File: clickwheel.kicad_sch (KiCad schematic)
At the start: 4 parts

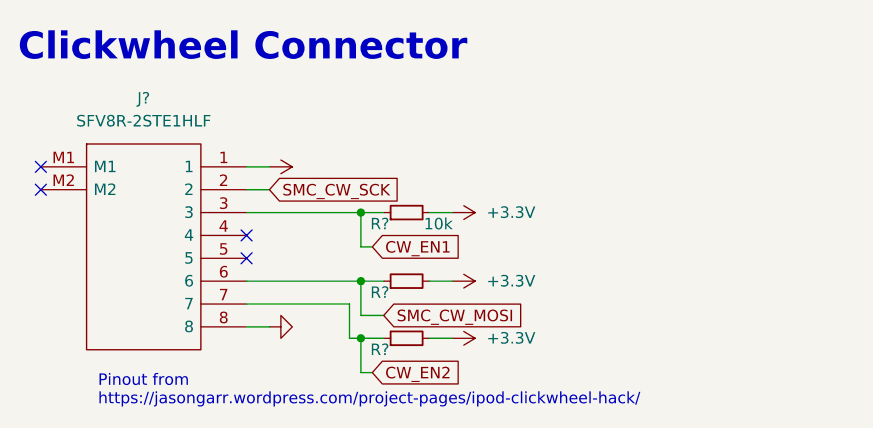
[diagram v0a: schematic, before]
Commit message: schem: first pass done, ERC passing
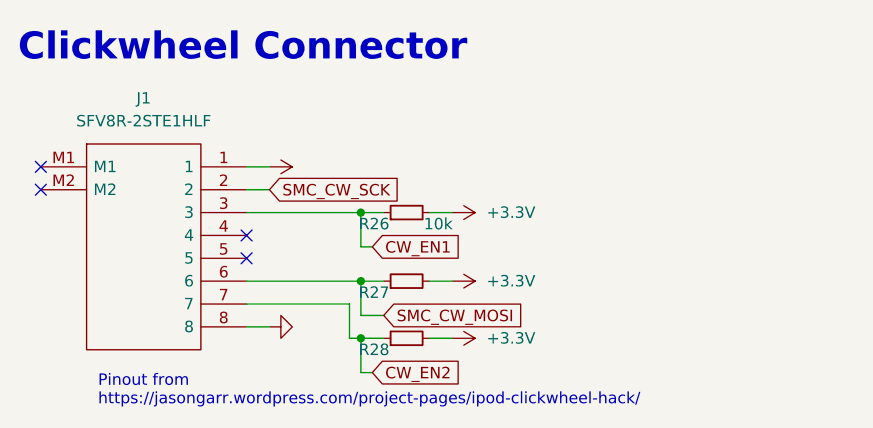
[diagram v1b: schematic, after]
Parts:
- gave numbers to parts that had none: 4
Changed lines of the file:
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@@
   (no_connect (at 95.25 88.9))
   (no_connect (at 95.25 91.44))
+  (no_connect (at 118.11 96.52))
   (no_connect (at 118.11 99.06))
-  (no_connect (at 118.11 96.52))
   (wire (pts (xy 132.08 111.76) (xy 130.81 111.76))
     (stroke (width 0) (type default) (color 0 0 0 0))
@@
   (symbol (lib_id "power:+3.3V") (at 140.97 93.98 270) (unit 1)
     (in_bom yes) (on_board yes) (fields_autoplaced)
-    (property "Reference" "#PWR?" (id 0) (at 137.16 93.98 0)
+    (property "Reference" "#PWR063" (id 0) (at 137.16 93.98 0)
       (effects (font (size 1.27 1.27)) hide)
     )
@@
   (symbol (lib_id "power:GND") (at 120.65 106.68 90) (unit 1)
     (in_bom yes) (on_board yes) (fields_autoplaced)
-    (property "Reference" "#PWR?" (id 0) (at 127 106.68 0)
+    (property "Reference" "#PWR062" (id 0) (at 127 106.68 0)
       (effects (font (size 1.27 1.27)) hide)
     )
@@
   (symbol (lib_id "Device:R_Small") (at 135.89 93.98 90) (unit 1)
     (in_bom yes) (on_board yes)
-    (property "Reference" "R?" (id 0) (at 133.985 95.25 90)
+    (property "Reference" "R26" (id 0) (at 133.985 95.25 90)
       (effects (font (size 1.27 1.27)) (justify left))
     )
@@
   (symbol (lib_id "Device:R_Small") (at 135.89 107.95 90) (unit 1)
     (in_bom yes) (on_board yes)
-    (property "Reference" "R?" (id 0) (at 133.985 109.22 90)
+    (property "Reference" "R28" (id 0) (at 133.985 109.22 90)
       (effects (font (size 1.27 1.27)) (justify left))
     )
@@
   (symbol (lib_id "gigahawk:SFV8R-2STE1HLF") (at 95.25 88.9 0) (unit 1)
     (in_bom yes) (on_board yes) (fields_autoplaced)
-    (property "Reference" "J?" (id 0) (at 106.68 81.28 0))
+    (property "Reference" "J1" (id 0) (at 106.68 81.28 0))
     (property "Value" "SFV8R-2STE1HLF" (id 1) (at 106.68 83.82 0))
     (property "Footprint" "Gigahawk:SFV8R2STE1HLF" (id 2) (at 114.3 86.36 0)
@@
   (symbol (lib_id "power:+3.3V") (at 120.65 88.9 270) (unit 1)
     (in_bom yes) (on_board yes) (fields_autoplaced)
-    (property "Reference" "#PWR?" (id 0) (at 116.84 88.9 0)
+    (property "Reference" "#PWR061" (id 0) (at 116.84 88.9 0)
       (effects (font (size 1.27 1.27)) hide)
     )
@@
   (symbol (lib_id "power:+3.3V") (at 140.97 101.6 270) (unit 1)
     (in_bom yes) (on_board yes) (fields_autoplaced)
-    (property "Reference" "#PWR?" (id 0) (at 137.16 101.6 0)
+    (property "Reference" "#PWR064" (id 0) (at 137.16 101.6 0)
       (effects (font (size 1.27 1.27)) hide)
     )
@@
   (symbol (lib_id "power:+3.3V") (at 140.97 107.95 270) (unit 1)
     (in_bom yes) (on_board yes) (fields_autoplaced)
-    (property "Reference" "#PWR?" (id 0) (at 137.16 107.95 0)
+    (property "Reference" "#PWR065" (id 0) (at 137.16 107.95 0)
       (effects (font (size 1.27 1.27)) hide)
     )
@@
   (symbol (lib_id "Device:R_Small") (at 135.89 101.6 90) (unit 1)
     (in_bom yes) (on_board yes)
-    (property "Reference" "R?" (id 0) (at 133.985 102.87 90)
-      (effects (font (size 1.27 1.27)) (justify left))
-    )
+    (property "Reference" "R27" (id 0) (at 133.985 102.87 90)
+      (effects (font (size 1.27 1.27)) (justify left))
+    )

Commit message: analysis: specify pi will be powered directly from VCC
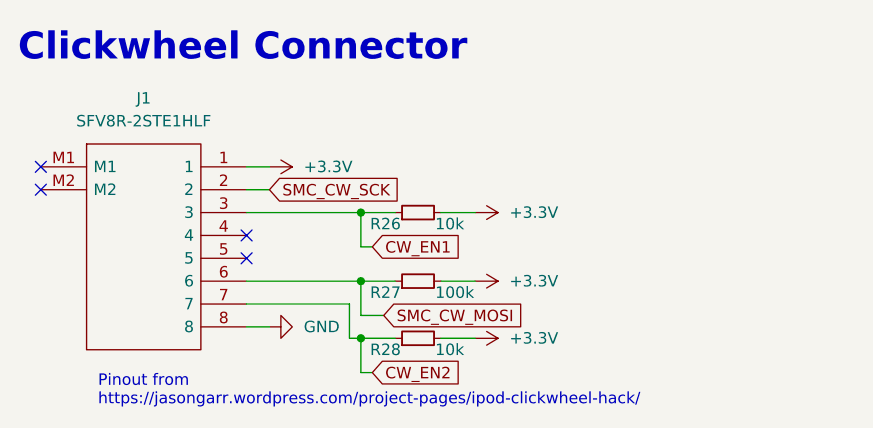
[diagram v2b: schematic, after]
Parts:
- R26: footprint (none) -> Resistor_SMD:R_0402_1005Metric
- R27: value (none) -> 100k; footprint (none) -> Resistor_SMD:R_0402_1005Metric
- R28: value (none) -> 10k; footprint (none) -> Resistor_SMD:R_0402_1005Metric
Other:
- moved on the sheet: R26, R27, R28
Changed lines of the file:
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@@
 (kicad_sch (version 20211123) (generator eeschema)
   (paper "A4")
+  (junction (at 130.81 107.95) (diameter 0) (color 0 0 0 0)
+  )
   (junction (at 130.81 93.98) (diameter 0) (color 0 0 0 0)
   )
   (junction (at 130.81 101.6) (diameter 0) (color 0 0 0 0)
-  )
-  (junction (at 130.81 107.95) (diameter 0) (color 0 0 0 0)
   )
   (no_connect (at 95.25 88.9))
@@
     (stroke (width 0) (type default) (color 0 0 0 0))
   )
-  (wire (pts (xy 130.81 101.6) (xy 133.35 101.6))
-    (stroke (width 0) (type default) (color 0 0 0 0))
-  )
-  (wire (pts (xy 129.54 107.95) (xy 130.81 107.95))
-    (stroke (width 0) (type default) (color 0 0 0 0))
-  )
-  (wire (pts (xy 130.81 93.98) (xy 133.35 93.98))
-    (stroke (width 0) (type default) (color 0 0 0 0))
-  )
-  (wire (pts (xy 138.43 107.95) (xy 140.97 107.95))
+  (wire (pts (xy 130.81 101.6) (xy 134.62 101.6))
+    (stroke (width 0) (type default) (color 0 0 0 0))
+  )
+  (wire (pts (xy 130.81 107.95) (xy 129.54 107.95))
+    (stroke (width 0) (type default) (color 0 0 0 0))
+  )
+  (wire (pts (xy 130.81 93.98) (xy 134.62 93.98))
+    (stroke (width 0) (type default) (color 0 0 0 0))
+  )
+  (wire (pts (xy 139.7 107.95) (xy 143.51 107.95))
     (stroke (width 0) (type default) (color 0 0 0 0))
   )
@@
     (stroke (width 0) (type default) (color 0 0 0 0))
   )
+  (wire (pts (xy 130.81 107.95) (xy 134.62 107.95))
+    (stroke (width 0) (type default) (color 0 0 0 0))
+  )
   (wire (pts (xy 130.81 97.79) (xy 130.81 93.98))
     (stroke (width 0) (type default) (color 0 0 0 0))
   )
-  (wire (pts (xy 138.43 93.98) (xy 140.97 93.98))
-    (stroke (width 0) (type default) (color 0 0 0 0))
-  )
-  (wire (pts (xy 138.43 101.6) (xy 140.97 101.6))
+  (wire (pts (xy 139.7 93.98) (xy 143.51 93.98))
+    (stroke (width 0) (type default) (color 0 0 0 0))
+  )
+  (wire (pts (xy 139.7 101.6) (xy 143.51 101.6))
     (stroke (width 0) (type default) (color 0 0 0 0))
   )
@@
   )
   (wire (pts (xy 118.11 104.14) (xy 129.54 104.14))
-    (stroke (width 0) (type default) (color 0 0 0 0))
-  )
-  (wire (pts (xy 130.81 107.95) (xy 133.35 107.95))
     (stroke (width 0) (type default) (color 0 0 0 0))
   )
@@
     )
   )
-  (symbol (lib_id "power:+3.3V") (at 140.97 93.98 270) (unit 1)
-    (in_bom yes) (on_board yes) (fields_autoplaced)
-    (property "Reference" "#PWR063" (id 0) (at 137.16 93.98 0)
-      (effects (font (size 1.27 1.27)) hide)
-    )
-    (property "Value" "+3.3V" (id 1) (at 144.78 93.9799 90)
-      (effects (font (size 1.27 1.27)) (justify left))
-    )
-    (property "Footprint" "" (id 2) (at 140.97 93.98 0)
-      (effects (font (size 1.27 1.27)) hide)
-    )
-    (property "Datasheet" "" (id 3) (at 140.97 93.98 0)
+  (symbol (lib_id "power:+3.3V") (at 143.51 93.98 270) (unit 1)
+    (in_bom yes) (on_board yes) (fields_autoplaced)
+    (property "Reference" "#PWR063" (id 0) (at 139.7 93.98 0)
+      (effects (font (size 1.27 1.27)) hide)
+    )
+    (property "Value" "+3.3V" (id 1) (at 147.32 93.9799 90)
+      (effects (font (size 1.27 1.27)) (justify left))
+    )
+    (property "Footprint" "" (id 2) (at 143.51 93.98 0)
+      (effects (font (size 1.27 1.27)) hide)
+    )
+    (property "Datasheet" "" (id 3) (at 143.51 93.98 0)
       (effects (font (size 1.27 1.27)) hide)
     )
@@
       (effects (font (size 1.27 1.27)) hide)
     )
-    (property "Value" "" (id 1) (at 124.46 106.6799 90)
+    (property "Value" "GND" (id 1) (at 124.46 106.6799 90)
       (effects (font (size 1.27 1.27)) (justify right))
     )
@@
     (pin "1")
   )
-  (symbol (lib_id "Device:R_Small") (at 135.89 93.98 90) (unit 1)
+  (symbol (lib_id "Device:R_Small") (at 137.16 93.98 90) (unit 1)
     (in_bom yes) (on_board yes)
-    (property "Reference" "R26" (id 0) (at 133.985 95.25 90)
-      (effects (font (size 1.27 1.27)) (justify left))
-    )
-    (property "Value" "10k" (id 1) (at 137.795 95.25 90)
-      (effects (font (size 1.27 1.27)) (justify right))
-    )
-    (property "Footprint" "" (id 2) (at 135.89 93.98 0)
-      (effects (font (size 1.27 1.27)) hide)
-    )
-    (property "Datasheet" "~" (id 3) (at 135.89 93.98 0)
+    (property "Reference" "R26" (id 0) (at 135.255 95.25 90)
+      (effects (font (size 1.27 1.27)) (justify left))
+    )
+    (property "Value" "10k" (id 1) (at 139.065 95.25 90)
+      (effects (font (size 1.27 1.27)) (justify right))
+    )
+    (property "Footprint" "Resistor_SMD:R_0402_1005Metric" (id 2) (at 137.16 93.98 0)
+      (effects (font (size 1.27 1.27)) hide)
+    )
+    (property "Datasheet" "~" (id 3) (at 137.16 93.98 0)
       (effects (font (size 1.27 1.27)) hide)
     )
@@
     (pin "2")
   )
-  (symbol (lib_id "Device:R_Small") (at 135.89 107.95 90) (unit 1)
+  (symbol (lib_id "Device:R_Small") (at 137.16 107.95 90) (unit 1)
     (in_bom yes) (on_board yes)
-    (property "Reference" "R28" (id 0) (at 133.985 109.22 90)
-      (effects (font (size 1.27 1.27)) (justify left))
-    )
-    (property "Value" "" (id 1) (at 137.795 109.22 90)
-      (effects (font (size 1.27 1.27)) (justify right))
-    )
-    (property "Footprint" "" (id 2) (at 135.89 107.95 0)
-      (effects (font (size 1.27 1.27)) hide)
-    )
-    (property "Datasheet" "~" (id 3) (at 135.89 107.95 0)
+    (property "Reference" "R28" (id 0) (at 135.255 109.22 90)
+      (effects (font (size 1.27 1.27)) (justify left))
+    )
+    (property "Value" "10k" (id 1) (at 139.065 109.22 90)
+      (effects (font (size 1.27 1.27)) (justify right))
+    )
+    (property "Footprint" "Resistor_SMD:R_0402_1005Metric" (id 2) (at 137.16 107.95 0)
+      (effects (font (size 1.27 1.27)) hide)
+    )
+    (property "Datasheet" "~" (id 3) (at 137.16 107.95 0)
       (effects (font (size 1.27 1.27)) hide)
     )
@@
       (effects (font (size 1.27 1.27)) hide)
     )
-    (property "Value" "" (id 1) (at 124.46 88.8999 90)
+    (property "Value" "+3.3V" (id 1) (at 124.46 88.8999 90)
       (effects (font (size 1.27 1.27)) (justify left))
     )
@@
     (pin "1")
   )
-  (symbol (lib_id "power:+3.3V") (at 140.97 101.6 270) (unit 1)
-    (in_bom yes) (on_board yes) (fields_autoplaced)
-    (property "Reference" "#PWR064" (id 0) (at 137.16 101.6 0)
-      (effects (font (size 1.27 1.27)) hide)
-    )
-    (property "Value" "+3.3V" (id 1) (at 144.78 101.5999 90)
-      (effects (font (size 1.27 1.27)) (justify left))
-    )
-    (property "Footprint" "" (id 2) (at 140.97 101.6 0)
-      (effects (font (size 1.27 1.27)) hide)
-    )
-    (property "Datasheet" "" (id 3) (at 140.97 101.6 0)
-      (effects (font (size 1.27 1.27)) hide)
-    )
-    (pin "1")
-  )
-  (symbol (lib_id "power:+3.3V") (at 140.97 107.95 270) (unit 1)
-    (in_bom yes) (on_board yes) (fields_autoplaced)
-    (property "Reference" "#PWR065" (id 0) (at 137.16 107.95 0)
-      (effects (font (size 1.27 1.27)) hide)
-    )
-    (property "Value" "+3.3V" (id 1) (at 144.78 107.9499 90)
-      (effects (font (size 1.27 1.27)) (justify left))
-    )
-    (property "Footprint" "" (id 2) (at 140.97 107.95 0)
-      (effects (font (size 1.27 1.27)) hide)
-    )
-    (property "Datasheet" "" (id 3) (at 140.97 107.95 0)
-      (effects (font (size 1.27 1.27)) hide)
-    )
-    (pin "1")
-  )
-  (symbol (lib_id "Device:R_Small") (at 135.89 101.6 90) (unit 1)
+  (symbol (lib_id "power:+3.3V") (at 143.51 101.6 270) (unit 1)
+    (in_bom yes) (on_board yes) (fields_autoplaced)
+    (property "Reference" "#PWR064" (id 0) (at 139.7 101.6 0)
+      (effects (font (size 1.27 1.27)) hide)
+    )
+    (property "Value" "+3.3V" (id 1) (at 147.32 101.5999 90)
+      (effects (font (size 1.27 1.27)) (justify left))
+    )
+    (property "Footprint" "" (id 2) (at 143.51 101.6 0)
+      (effects (font (size 1.27 1.27)) hide)
+    )
+    (property "Datasheet" "" (id 3) (at 143.51 101.6 0)
+      (effects (font (size 1.27 1.27)) hide)
+    )
+    (pin "1")
+  )
+  (symbol (lib_id "power:+3.3V") (at 143.51 107.95 270) (unit 1)
+    (in_bom yes) (on_board yes) (fields_autoplaced)
+    (property "Reference" "#PWR065" (id 0) (at 139.7 107.95 0)
+      (effects (font (size 1.27 1.27)) hide)
+    )
+    (property "Value" "+3.3V" (id 1) (at 147.32 107.9499 90)
+      (effects (font (size 1.27 1.27)) (justify left))
+    )
+    (property "Footprint" "" (id 2) (at 143.51 107.95 0)
+      (effects (font (size 1.27 1.27)) hide)
+    )
+    (property "Datasheet" "" (id 3) (at 143.51 107.95 0)
+      (effects (font (size 1.27 1.27)) hide)
+    )
+    (pin "1")
+  )
+  (symbol (lib_id "Device:R_Small") (at 137.16 101.6 90) (unit 1)
     (in_bom yes) (on_board yes)
-    (property "Reference" "R27" (id 0) (at 133.985 102.87 90)
-      (effects (font (size 1.27 1.27)) (justify left))
-    )
-    (property "Value" "" (id 1) (at 137.795 102.87 90)
-      (effects (font (size 1.27 1.27)) (justify right))
-    )
-    (property "Footprint" "" (id 2) (at 135.89 101.6 0)
-      (effects (font (size 1.27 1.27)) hide)
-    )
-    (property "Datasheet" "~" (id 3) (at 135.89 101.6 0)
-      (effects (font (size 1.27 1.27)) hide)
-    )
+    (property "Reference" "R27" (id 0) (at 135.255 102.87 90)
+      (effects (font (size 1.27 1.27)) (justify left))
+    )
+    (property "Value" "100k" (id 1) (at 139.065 102.87 90)
+      (effects (font (size 1.27 1.27)) (justify right))
+    )
+    (property "Footprint" "Resistor_SMD:R_0402_1005Metric" (id 2) (at 137.16 101.6 0)
+      (effects (font (size 1.27 1.27)) hide)
+    )
+    (property "Datasheet" "~" (id 3) (at 137.16 101.6 0)
+      (effects (font (size 1.27 1.27)) hide)
+    )

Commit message: layout: switch to lcsc fpc connectors
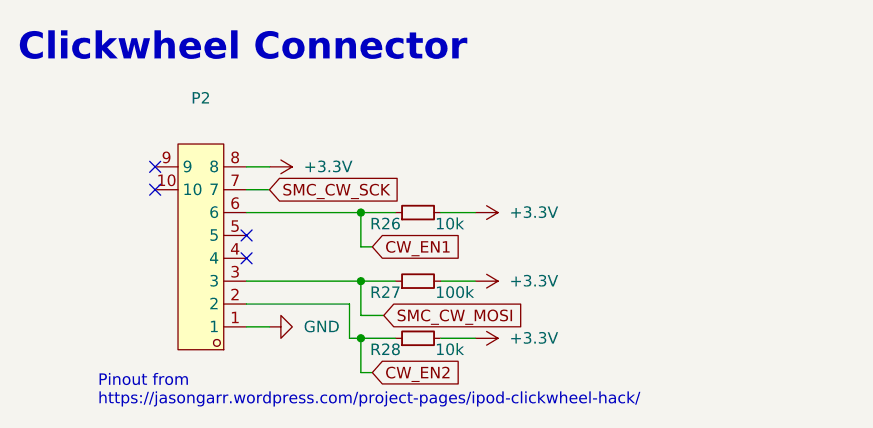
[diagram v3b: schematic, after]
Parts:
- removed J1: SFV8R-2STE1HLF, Gigahawk:SFV8R2STE1HLF, symbol gigahawk:SFV8R-2STE1HLF
- added P2: (no value), symbol lcsc:FPC0.5MM8PPulltypeH2.0mmPickup
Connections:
- net +3V3: now also P2.8
- net CW_EN1: now also P2.6
- net CW_EN2: now also P2.2
- net GND: now also P2.1
- net SMC_CW_MOSI: now also P2.3
- net SMC_CW_SCK: now also P2.7
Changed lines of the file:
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@@
   (junction (at 130.81 101.6) (diameter 0) (color 0 0 0 0)
   )
-  (no_connect (at 95.25 88.9))
-  (no_connect (at 95.25 91.44))
+  (no_connect (at 107.95 88.9))
+  (no_connect (at 107.95 91.44))
   (no_connect (at 118.11 96.52))
   (no_connect (at 118.11 99.06))
@@
     )
   )
+  (symbol (lib_id "lcsc:FPC0.5MM8PPulltypeH2.0mmPickup") (at 114.3 97.79 180) (unit 1)
+    (in_bom yes) (on_board yes) (fields_autoplaced)
+    (property "Reference" "P2" (id 0) (at 113.03 81.28 0))
+    (property "Value" "" (id 1) (at 113.03 83.82 0))
+    (property "Footprint" "" (id 2) (at 114.3 81.28 0)
+      (effects (font (size 1.27 1.27)) hide)
+    )
+    (property "Datasheet" "https://lcsc.com/product-detail/FPC-Connectors_FPC-0-5mmpitch-8P-H2-0mm-Pull-type-Pick-up_C11084.html" (id 3) (at 114.3 78.74 0)
+      (effects (font (size 1.27 1.27)) hide)
+    )
+    (property "Manufacturer" "ReliaPro" (id 4) (at 114.3 76.2 0)
+      (effects (font (size 1.27 1.27)) hide)
+    )
+    (property "LCSC Part" "C11084" (id 5) (at 114.3 73.66 0)
+      (effects (font (size 1.27 1.27)) hide)
+    )
+    (property "JLC Part" "Extended Part" (id 6) (at 114.3 71.12 0)
+      (effects (font (size 1.27 1.27)) hide)
+    )
+    (pin "1")
+    (pin "10")
+    (pin "2")
+    (pin "3")
+    (pin "4")
+    (pin "5")
+    (pin "6")
+    (pin "7")
+    (pin "8")
+    (pin "9")
+  )
   (symbol (lib_id "power:+3.3V") (at 143.51 93.98 270) (unit 1)
     (in_bom yes) (on_board yes) (fields_autoplaced)
@@
     (pin "2")
   )
-  (symbol (lib_id "gigahawk:SFV8R-2STE1HLF") (at 95.25 88.9 0) (unit 1)
-    (in_bom yes) (on_board yes) (fields_autoplaced)
-    (property "Reference" "J1" (id 0) (at 106.68 81.28 0))
-    (property "Value" "SFV8R-2STE1HLF" (id 1) (at 106.68 83.82 0))
-    (property "Footprint" "Gigahawk:SFV8R2STE1HLF" (id 2) (at 114.3 86.36 0)
-      (effects (font (size 1.27 1.27)) (justify left) hide)
-    )
-    (property "Datasheet" "https://cdn.amphenol-icc.com/media/wysiwyg/files/drawing/10112793.pdf" (id 3) (at 114.3 88.9 0)
-      (effects (font (size 1.27 1.27)) (justify left) hide)
-    )
-    (property "Description" "FFC & FPC Connectors FFC/FPC CONN" (id 4) (at 114.3 91.44 0)
-      (effects (font (size 1.27 1.27)) (justify left) hide)
-    )
-    (property "Height" "2" (id 5) (at 114.3 93.98 0)
-      (effects (font (size 1.27 1.27)) (justify left) hide)
-    )
-    (property "Mouser Part Number" "649-SFV8R-2STE1HLF" (id 6) (at 114.3 96.52 0)
-      (effects (font (size 1.27 1.27)) (justify left) hide)
-    )
-    (property "Mouser Price/Stock" "https://www.mouser.co.uk/ProductDetail/Amphenol-FCI/SFV8R-2STE1HLF?qs=SqJKR5Mmryfw9HHOb%2F1Fzg%3D%3D" (id 7) (at 114.3 99.06 0)
-      (effects (font (size 1.27 1.27)) (justify left) hide)
-    )
-    (property "Manufacturer_Name" "Amphenol" (id 8) (at 114.3 101.6 0)
-      (effects (font (size 1.27 1.27)) (justify left) hide)
-    )
-    (property "Manufacturer_Part_Number" "SFV8R-2STE1HLF" (id 9) (at 114.3 104.14 0)
-      (effects (font (size 1.27 1.27)) (justify left) hide)
-    )
-    (pin "1")
-    (pin "2")
-    (pin "3")
-    (pin "4")
-    (pin "5")
-    (pin "6")
-    (pin "7")
-    (pin "8")
-    (pin "M1")
-    (pin "M2")
-  )
   (symbol (lib_id "power:+3.3V") (at 120.65 88.9 270) (unit 1)

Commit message: integration: add mounting holes and connectors and second board
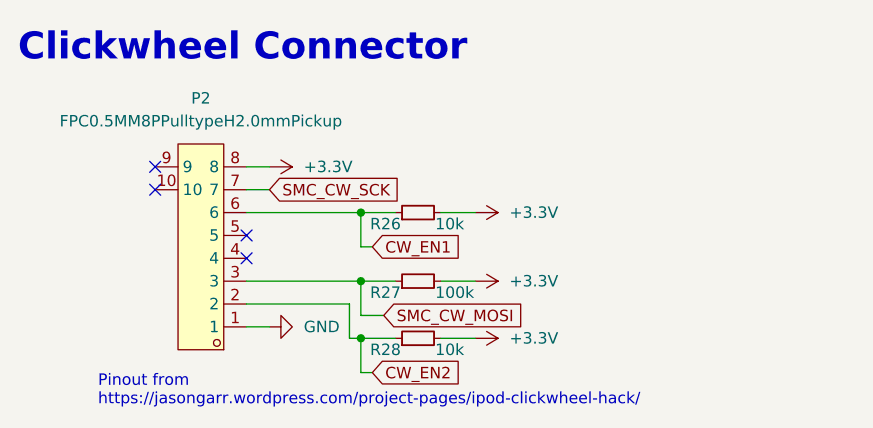
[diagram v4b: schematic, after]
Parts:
- P2: value (none) -> FPC0.5MM8PPulltypeH2.0mmPickup; footprint (none) -> lcsc:FPC-SMD_AFC07-S08ECC-00
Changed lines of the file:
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@@
     (in_bom yes) (on_board yes) (fields_autoplaced)
     (property "Reference" "P2" (id 0) (at 113.03 81.28 0))
-    (property "Value" "" (id 1) (at 113.03 83.82 0))
-    (property "Footprint" "" (id 2) (at 114.3 81.28 0)
+    (property "Value" "FPC0.5MM8PPulltypeH2.0mmPickup" (id 1) (at 113.03 83.82 0))
+    (property "Footprint" "lcsc:FPC-SMD_AFC07-S08ECC-00" (id 2) (at 114.3 81.28 0)
       (effects (font (size 1.27 1.27)) hide)
     )
